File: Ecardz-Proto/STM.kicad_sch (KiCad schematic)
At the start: 30 parts, among them J1 Conn_02x06_Odd_Even, J3 Conn_ARM_SWD_TagConnect_TC203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, J4 Conn_02x07_Odd_Even, U1 STM32L071K8Ux

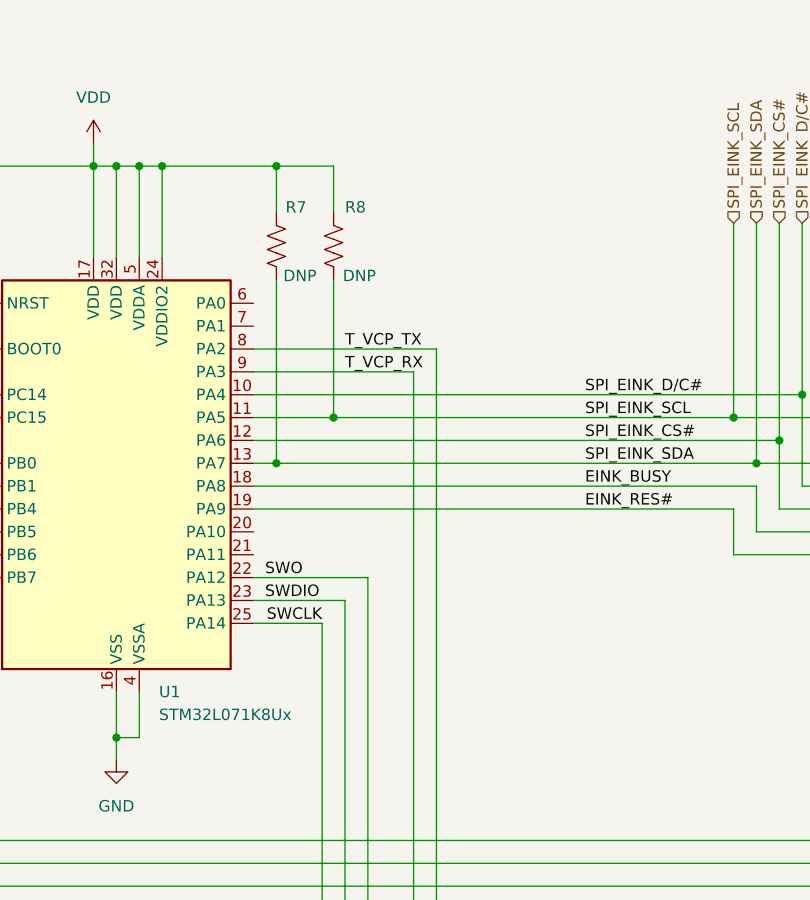
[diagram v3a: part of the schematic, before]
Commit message: made all supply voltages VDD rather than mix of VDD/VCC, added VDD measurement via STM32 internal ADC, put DNP jumper for VPP on E-ink connector, and made NFC VCC pin only connected to power if externally powered
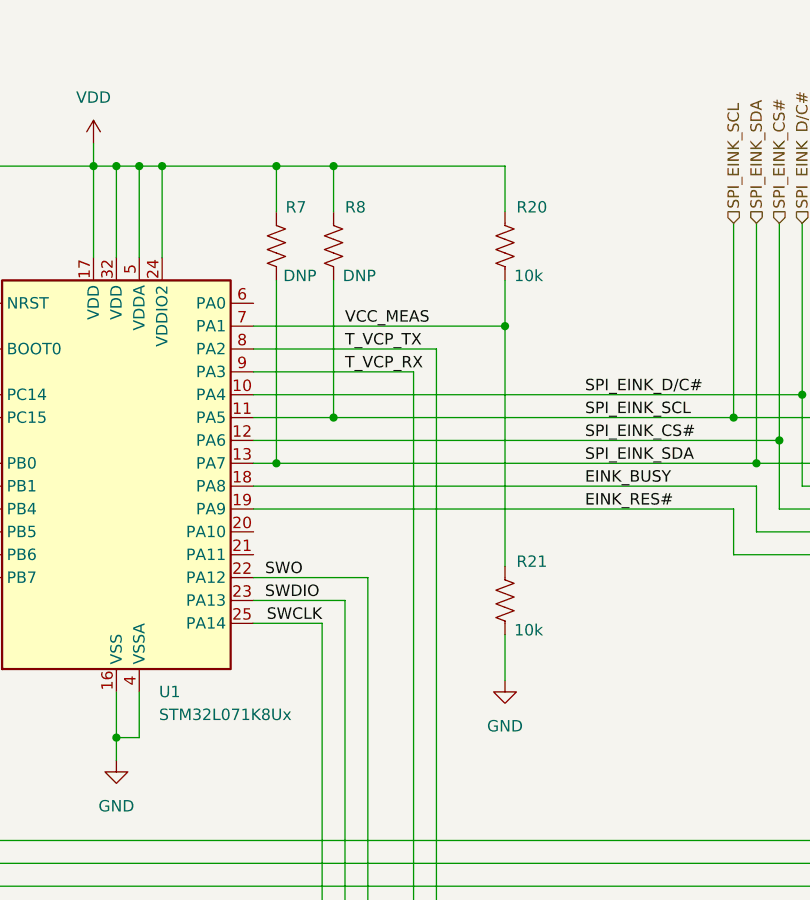
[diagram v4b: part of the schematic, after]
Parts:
- added R20, R21: 10k, Resistor_SMD:R_0603_1608Metric_Pad0.98x0.95mm_HandSolder, symbol Device:R_US
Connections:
- net GND: now also R21.2
- net VDD: now also R20.1
- net VCC_MEAS: now reaches U1.7 (PA1)
- net VCC_MEAS: now also R20.2, R21.1

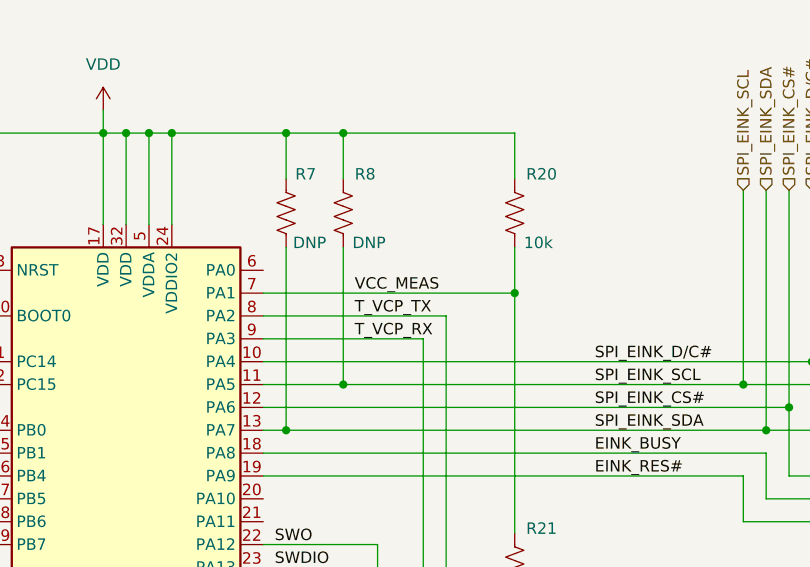
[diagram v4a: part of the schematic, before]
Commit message: added jumpers to select NFC chip's power supply connection
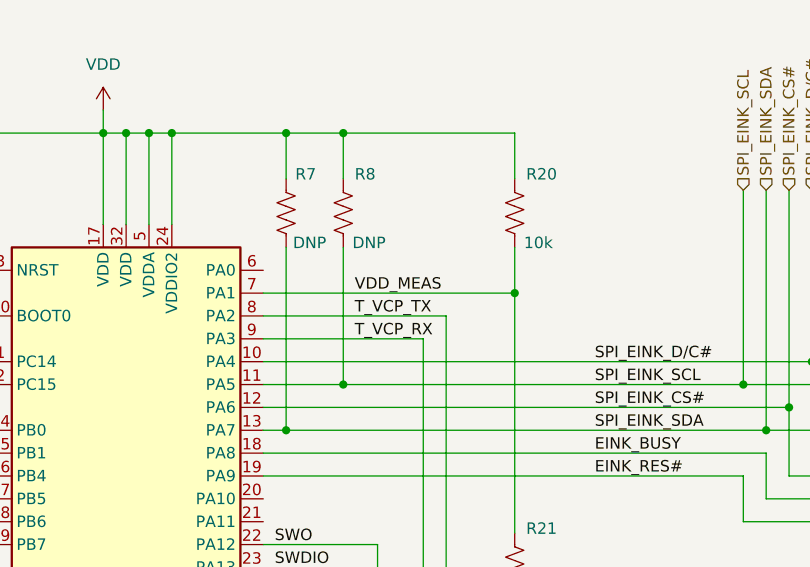
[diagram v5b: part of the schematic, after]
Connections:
- net VCC_MEAS renamed VDD_MEAS
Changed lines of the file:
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@@
 		)
 	)
-	(label "VCC_MEAS"
+	(label "VDD_MEAS"
 		(at 118.11 91.44 0)
 		(fields_autoplaced yes)

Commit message: updated most footprints
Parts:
- added J5: Conn_01x05, Connector_PCBEdge:Samtec_MECF-05-0_-NP-L-DV_2x05_P1.27mm_Edge, symbol Connector_Generic:Conn_01x05
- J1: footprint (none) -> Connector_PinHeader_2.54mm:PinHeader_2x06_P2.54mm_Vertical
- J4: footprint (none) -> Connector_PinSocket_1.27mm:PinSocket_2x07_P1.27mm_Vertical_SMD
- TP1, TP11, TP12, TP13, TP14, TP2, TP3, TP4, TP5, TP6, TP9: footprint (none) -> TestPoint:TestPoint_Pad_3.0x3.0mm
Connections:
- net GND: now also J5.5 (Pin_5)
- net NRST_TAG: now also J5.4 (Pin_4)
- net SWCLK_TAG: now also J5.3 (Pin_3)
- net SWDIO_TAG: now also J5.2 (Pin_2)
- net VDD: now also J5.1 (Pin_1)
- no-connect marks 4 -> 5

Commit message: board outline
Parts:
- added C17, C18, C19: 1uF, Capacitor_SMD:C_0603_1608Metric_Pad1.08x0.95mm_HandSolder, symbol Device:C
- TP1, TP11, TP12, TP13, TP14, TP2, TP3, TP4, TP5, TP6, TP9: footprint TestPoint:TestPoint_Pad_3.0x3.0mm -> TestPoint:TestPoint_Pad_1.0x1.0mm
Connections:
- net GND: now also C17.1, C18.1, C19.1
- net VDD: now also C17.2, C18.2, C19.2
- no-connect marks 5 -> 13

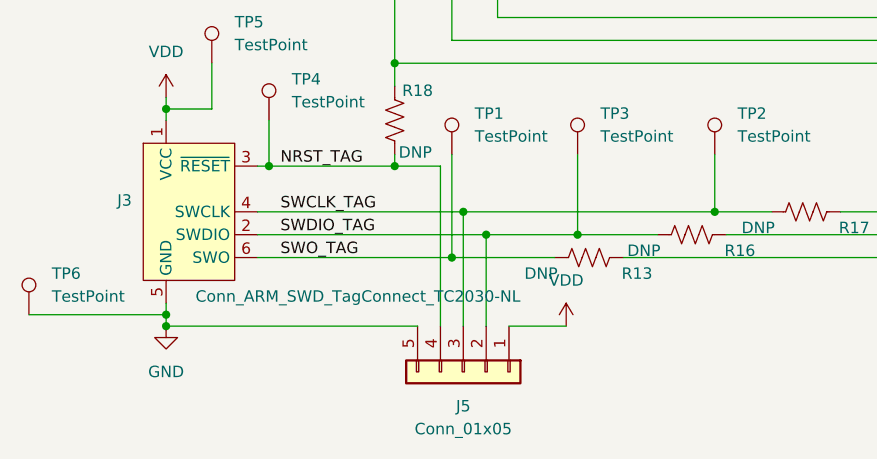
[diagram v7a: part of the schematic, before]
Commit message: rough layout complete
need to fix silkscreens and finish antenna
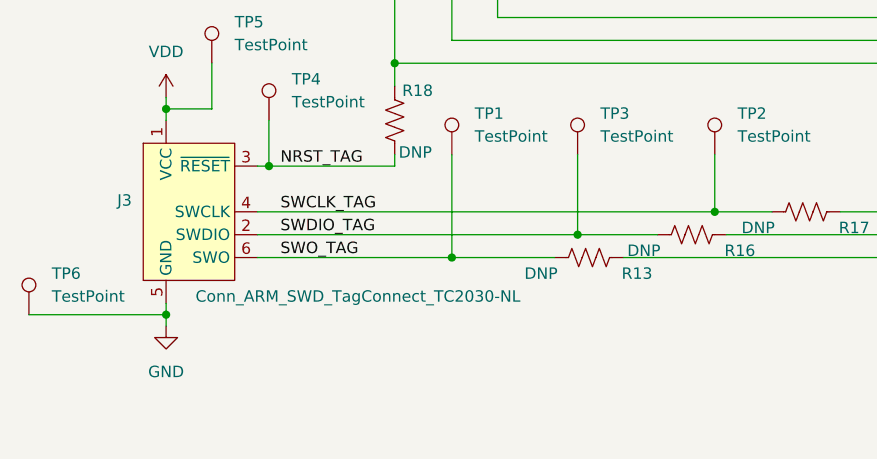
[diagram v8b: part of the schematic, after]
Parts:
- removed J5: Conn_01x05, Connector_PCBEdge:Samtec_MECF-05-0_-NP-L-DV_2x05_P1.27mm_Edge, symbol Connector_Generic:Conn_01x05
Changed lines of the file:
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@@
 	(paper "A4")
 	(junction
-		(at 66.04 172.72)
-		(diameter 0)
-		(color 0 0 0 0)
-	)
-	(junction
 		(at 44.45 167.64)
 		(diameter 0)
@@
 	)
 	(junction
-		(at 68.58 175.26)
-		(diameter 0)
-		(color 0 0 0 0)
-	)
-	(junction
 		(at 92.71 137.16)
 		(diameter 0)
@@
 	)
 	(junction
-		(at 33.02 185.42)
-		(diameter 0)
-		(color 0 0 0 0)
-	)
-	(junction
 		(at 40.64 73.66)
 		(diameter 0)
@@
 	)
 	(junction
-		(at 58.42 167.64)
-		(diameter 0)
-		(color 0 0 0 0)
-	)
-	(junction
 		(at 116.84 73.66)
 		(diameter 0)
@@
 	(wire
 		(pts
-			(xy 63.5 167.64) (xy 58.42 167.64)
-		)
-		(stroke
-			(width 0)
-			(type default)
-		)
-	)
-	(wire
-		(pts
 			(xy 26.67 116.84) (xy 35.56 116.84)
 		)
@@
 	(wire
 		(pts
-			(xy 66.04 172.72) (xy 93.98 172.72)
-		)
-		(stroke
-			(width 0)
-			(type default)
-		)
-	)
-	(wire
-		(pts
 			(xy 166.37 111.76) (xy 176.53 111.76)
 		)
@@
 	(wire
 		(pts
-			(xy 71.12 185.42) (xy 77.47 185.42)
-		)
-		(stroke
-			(width 0)
-			(type default)
-		)
-	)
-	(wire
-		(pts
 			(xy 58.42 156.21) (xy 113.03 156.21)
 		)
@@
 	(wire
 		(pts
-			(xy 43.18 175.26) (xy 68.58 175.26)
+			(xy 43.18 175.26) (xy 78.74 175.26)
 		)
 		(stroke
@@
 	(wire
 		(pts
-			(xy 60.96 185.42) (xy 33.02 185.42)
-		)
-		(stroke
-			(width 0)
-			(type default)
-		)
-	)
-	(wire
-		(pts
-			(xy 63.5 185.42) (xy 63.5 167.64)
-		)
-		(stroke
-			(width 0)
-			(type default)
-		)
-	)
-	(wire
-		(pts
 			(xy 118.11 121.92) (xy 118.11 170.18)
 		)
@@
 	(wire
 		(pts
-			(xy 68.58 175.26) (xy 78.74 175.26)
-		)
-		(stroke
-			(width 0)
-			(type default)
-		)
-	)
-	(wire
-		(pts
 			(xy 107.95 99.06) (xy 168.91 99.06)
 		)
@@
 	(wire
 		(pts
-			(xy 68.58 175.26) (xy 68.58 185.42)
-		)
-		(stroke
-			(width 0)
-			(type default)
-		)
-	)
-	(wire
-		(pts
 			(xy 69.85 138.43) (xy 69.85 116.84)
 		)
@@
 	(wire
 		(pts
-			(xy 43.18 172.72) (xy 66.04 172.72)
+			(xy 43.18 172.72) (xy 93.98 172.72)
 		)
 		(stroke
@@
 	(wire
 		(pts
-			(xy 66.04 172.72) (xy 66.04 185.42)
-		)
-		(stroke
-			(width 0)
-			(type default)
-		)
-	)
-	(wire
-		(pts
 			(xy 163.83 114.3) (xy 171.45 114.3)
 		)
@@
 	)
 	(symbol
-		(lib_id "power:VDD")
-		(at 77.47 185.42 0)
-		(unit 1)
-		(exclude_from_sim no)
-		(in_bom yes)
-		(on_board yes)
-		(dnp no)
-		(fields_autoplaced yes)
-		(property "Reference" "#PWR022"
-			(at 77.47 189.23 0)
-			(effects
-				(font
-					(size 1.27 1.27)
-				)
-				(hide yes)
-			)
-		)
-		(property "Value" "VDD"
-			(at 77.47 180.34 0)
-			(effects
-				(font
-					(size 1.27 1.27)
-				)
-			)
-		)
-		(property "Footprint" ""
-			(at 77.47 185.42 0)
-			(effects
-				(font
-					(size 1.27 1.27)
-				)
-				(hide yes)
-			)
-		)
-		(property "Datasheet" ""
-			(at 77.47 185.42 0)
-			(effects
-				(font
-					(size 1.27 1.27)
-				)
-				(hide yes)
-			)
-		)
-		(property "Description" "Power symbol creates a global label with name \"VDD\""
-			(at 77.47 185.42 0)
-			(effects
-				(font
-					(size 1.27 1.27)
-				)
-				(hide yes)
-			)
-		)
-		(pin "1"
-		)
-		(instances
-			(project "Ecardz-Proto"
-				(path "/2adbba85-9270-4efb-857d-656bb51406ca/fb28d19f-d7f8-44fd-bba1-2dc19a83839b"
-					(reference "#PWR022")
-					(unit 1)
-				)
-			)
-		)
-	)
-	(symbol
 		(lib_id "Device:R_US")
 		(at 181.61 106.68 90)
@@
 					(unit 1)
 				)
-			)
-		)
-	)
-	(symbol
-		(lib_id "Connector_Generic:Conn_01x05")
-		(at 66.04 190.5 270)
-		(unit 1)
-		(exclude_from_sim no)
-		(in_bom yes)
-		(on_board yes)
-		(dnp no)
-		(fields_autoplaced yes)
-		(property "Reference" "J5"
-			(at 66.04 194.31 90)
-			(effects
-				(font
-					(size 1.27 1.27)
-				)
-			)
-		)
-		(property "Value" "Conn_01x05"
-			(at 66.04 196.85 90)
-			(effects
-				(font
-					(size 1.27 1.27)
-				)
-			)
-		)
-		(property "Footprint" "Connector_PCBEdge:Samtec_MECF-05-0_-NP-L-DV_2x05_P1.27mm_Edge"
-			(at 66.04 190.5 0)
-			(effects
-				(font
-					(size 1.27 1.27)
-				)
-				(hide yes)
-			)
-		)
-		(property "Datasheet" "~"
-			(at 66.04 190.5 0)
-			(effects
-				(font
-					(size 1.27 1.27)
-				)
-				(hide yes)
-			)
-		)
-		(property "Description" "Generic connector, single row, 01x05, script generated (kicad-library-utils/schlib/autogen/connector/)"
-			(at 66.04 190.5 0)
-			(effects
-				(font
-					(size 1.27 1.27)
-				)
-				(hide yes)
-			)
-		)
-		(pin "5"
-		)
-		(pin "4"
-		)
-		(pin "3"
-		)
-		(pin "2"
-		)
-		(pin "1"
-		)
-		(instances
-			(project "Ecardz-Proto"
-				(path "/2adbba85-9270-4efb-857d-656bb51406ca/fb28d19f-d7f8-44fd-bba1-2dc19a83839b"
-					(reference "J5")
-					(unit 1)
-				)
